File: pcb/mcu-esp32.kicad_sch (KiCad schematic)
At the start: 5 parts, among them Q6 BSS138, U10 ESP32-S3-WROOM-1-N8R8

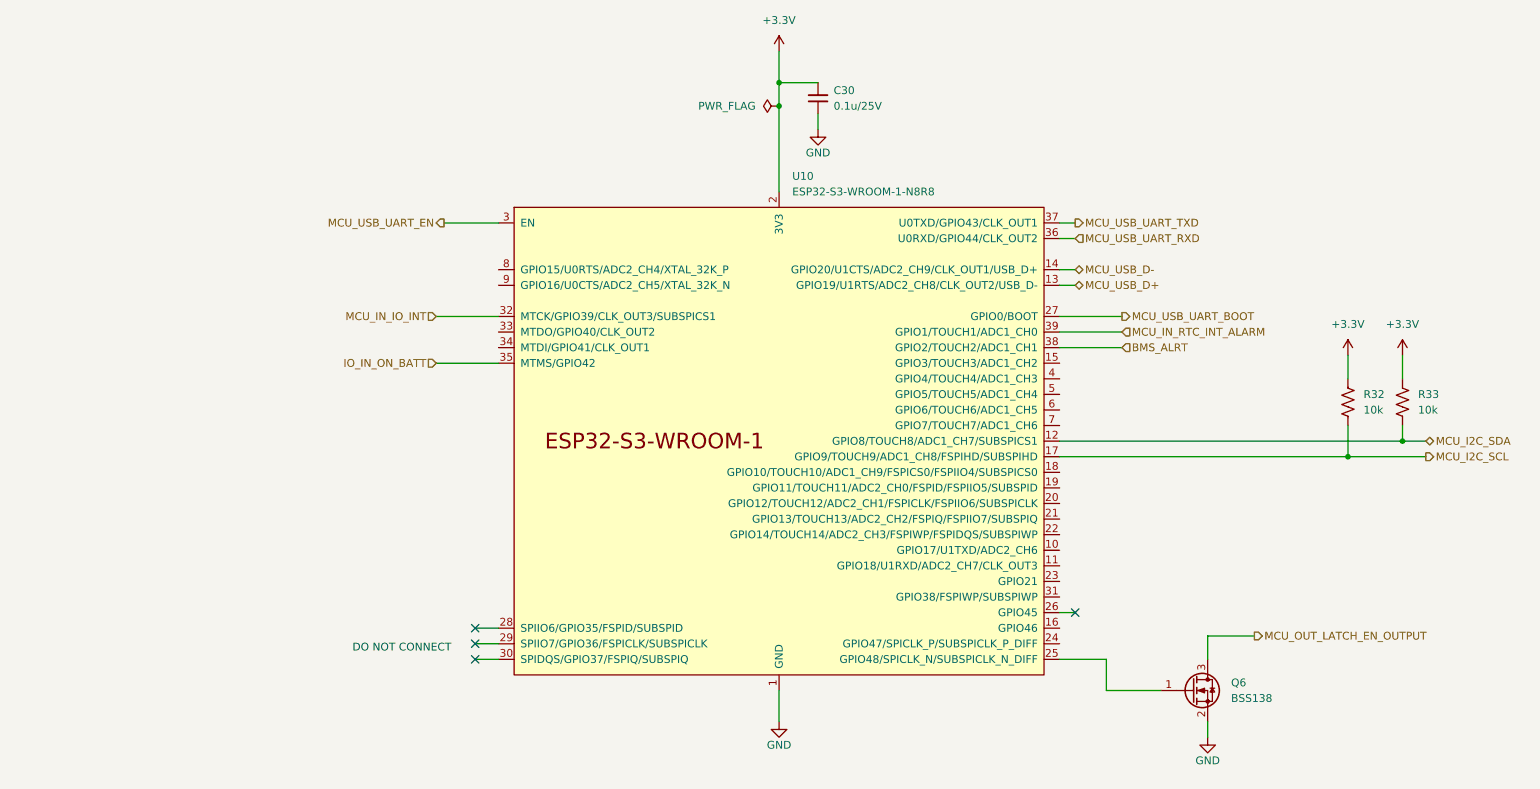
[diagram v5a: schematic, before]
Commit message: Wire SD card interface, fix R29/Q6/Q7 sourcing, localize datasheets project-wide
- SD card (Card1, Molex 472192001) wired to the FSPI (SPI2) peripheral:
  IO10/FSPICS0->CS, IO11/FSPID->MOSI, IO12/FSPICLK->SCLK, IO13/FSPIQ->MISO;
  shield/mounting tabs renamed SHLD and grounded; local decoupling cap added
- R29 was silently a 10k YAGEO part (RC0603FR-0710KL/C98220) sitting under a
  1M designator -- corrected to the real 1M part (RC0603FR-071ML/C105578),
  matching this rail's documented VRAW soft-latch bleed design intent
- Q6, Q7 (BSS138): added missing Manf/MPN/LCSC Part# (onsemi BSS138LT1G,
  C82045)
- C32/C36: normalized Value strings; fixed C36's Datasheet, which pointed to
  a different capacitor's PDF entirely
- Localized every remaining component's Datasheet field to a project-local
  path across all 8 schematic sheets (was a live remote URL before), per
  the new datasheet-localization task; caught and rejected a wrong-language
  and a wrong-manufacturer-clone source along the way (U8, U14, U15, Y2)
- Fixed 4 datasheet fields (Q1, D1, U6, U7) that had reverted from their
  already-localized paths back to remote URLs, apparently from a native
  KiCad symbol-library resync picking up stale library-level defaults

Co-Authored-By: Claude Sonnet 5 <noreply@anthropic.com>
Claude-Session: https://claude.ai/code/session_01LhLkuH6sQ5GbUZ61bG7p2h
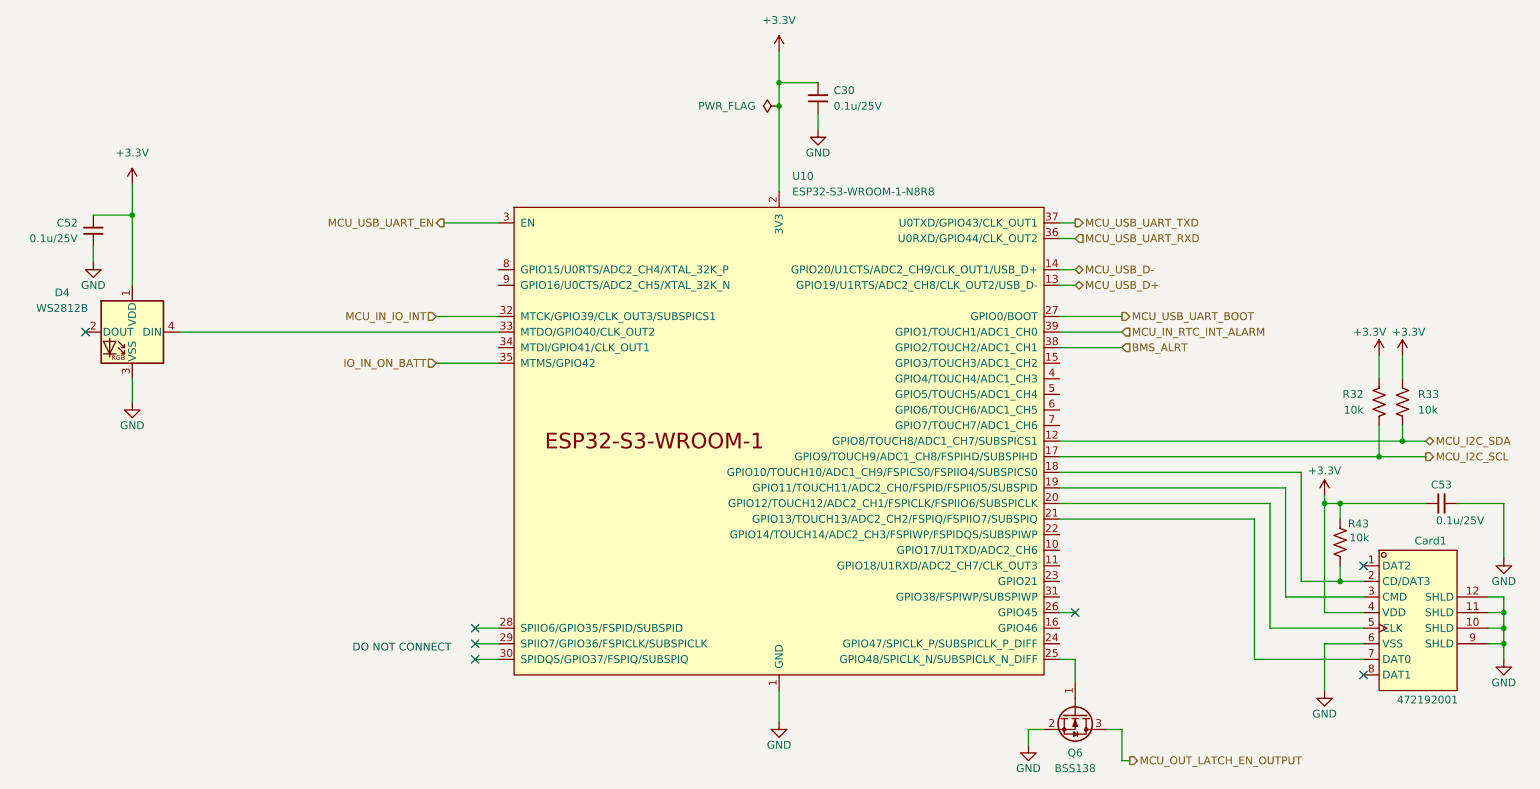
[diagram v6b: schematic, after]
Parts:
- added C52, C53: 0.1u/25V, Capacitor_SMD:C_0603_1608Metric, symbol Device:C_Small
- added Card1: 472192001, kicad_gx_library:TF-SMD_472192001, symbol kicad_gx_library:472192001
- added D4: WS2812B, LED_SMD:LED_WS2812B_PLCC4_5.0x5.0mm_P3.2mm, symbol LED:WS2812B
- added R43: 10k, Resistor_SMD:R_0603_1608Metric, symbol Device:R_US
- U10: footprint RF_Module:ESP32-S3-WROOM-1 -> PCM_Espressif:ESP32-S3-WROOM-1
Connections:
- net +3.3V: now also C52.1, C53.1, Card1.4 (VDD), D4.1 (VDD), R43.2
- net GND: now also C52.2, C53.2, Card1.10 (SHLD), Card1.11 (SHLD), Card1.12 (SHLD), Card1.6 (VSS), Card1.9 (SHLD), D4.3 (VSS)
- net at U10.18 (GPIO10/TOUCH10/ADC1_CH9/FSPICS0/FSPIIO4/SUBSPICS0): now also Card1.2 (CD/DAT3), R43.1
- net at U10.19 (GPIO11/TOUCH11/ADC2_CH0/FSPID/FSPIIO5/SUBSPID): now also Card1.3 (CMD)
- net at U10.20 (GPIO12/TOUCH12/ADC2_CH1/FSPICLK/FSPIIO6/SUBSPICLK): now also Card1.5 (CLK)
- net at U10.21 (GPIO13/TOUCH13/ADC2_CH2/FSPIQ/FSPIIO7/SUBSPIQ): now also Card1.7 (DAT0)
- net at U10.33 (MTDO/GPIO40/CLK_OUT2): now also D4.4 (DIN)
- no-connect marks 4 -> 7
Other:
- moved on the sheet: Q6, R32

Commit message: Fix remaining mass-symbol-update reversions (67 Datasheet + 5 Footprint fields)
The project-wide "Update Symbols from Library" run reverted far more than
the 4 caught in the previous commit -- most of that commit's own claimed
"localized project-wide" state was actually already the reverted state,
since the mass update happened before that commit and git history alone
couldn't detect it. Cross-referenced every component's Datasheet/Footprint
against the independent tracking docs (project_library_datasheets.md,
kicad_gx_library_datasheets.md, footprint_verification_log.md) instead.

- 67 components: Datasheet reverted from a localized ${KIPRJMOD} path back
  to a remote URL, across all 8 schematic files
- 5 components: Footprint also reverted, not just Datasheet -- Y2 (RTC
  crystal) reverted to a physically different package size (5.0x3.2mm vs.
  the real 3.2x1.5mm part); U9/U12 (LM1117 LDOs), U10 (ESP32-S3 module),
  and Y1 (12MHz crystal) reverted to differently-sourced but plausible
  footprints from a vendored library instead of the verified stock ones

No MPN/Manf/LCSC Part#/Value regressions found (checked all 185
components). ERC clean, same 15 pre-existing errors as before.

Co-Authored-By: Claude Sonnet 5 <noreply@anthropic.com>
Claude-Session: https://claude.ai/code/session_01LhLkuH6sQ5GbUZ61bG7p2h
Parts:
- U10: footprint PCM_Espressif:ESP32-S3-WROOM-1 -> RF_Module:ESP32-S3-WROOM-1
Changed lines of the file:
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@@
 			)
 		)
-		(property "Datasheet" "https://cdn-shop.adafruit.com/datasheets/WS2812B.pdf"
+		(property "Datasheet" "${KIPRJMOD}/project_library/datasheets/Worldsemi/WS2812B-B_W.pdf"
 			(at 38.1 108.585 0)
 			(hide yes)
@@
 			)
 		)
-		(property "Datasheet" "${KIPRJMOD}/project_library/datasheets/YAGEO/RC0805FR-0710KL.pdf"
+		(property "Datasheet" "${KIPRJMOD}/project_library/datasheets/YAGEO/RT0603BRD0710KL.pdf"
 			(at 243.84 110.49 0)
 			(hide yes)
@@
 			)
 		)
-		(property "Footprint" "PCM_Espressif:ESP32-S3-WROOM-1"
+		(property "Footprint" "RF_Module:ESP32-S3-WROOM-1"
 			(at 148.59 165.1 0)
 			(hide yes)
@@
 			)
 		)
-		(property "Datasheet" "https://www.espressif.com/sites/default/files/documentation/esp32-s3-wroom-1_wroom-1u_datasheet_en.pdf"
+		(property "Datasheet" "${KIPRJMOD}/project_library/datasheets/ESPRESSIF/ESP32-S3-WROOM-1-N8R8.pdf"
 			(at 148.59 167.64 0)
 			(hide yes)
@@
 			)
 		)
-		(property "Datasheet" "${KIPRJMOD}/project_library/datasheets/YAGEO/RC0805FR-0710KL.pdf"
+		(property "Datasheet" "${KIPRJMOD}/project_library/datasheets/YAGEO/RT0603BRD0710KL.pdf"
 			(at 247.65 110.49 0)
 			(hide yes)
@@
 			)
 		)
-		(property "Datasheet" "${KIPRJMOD}/project_library/datasheets/YAGEO/RC0805FR-0710KL.pdf"
+		(property "Datasheet" "${KIPRJMOD}/project_library/datasheets/YAGEO/RT0603BRD0710KL.pdf"
 			(at 237.49 133.35 0)
 			(hide yes)
